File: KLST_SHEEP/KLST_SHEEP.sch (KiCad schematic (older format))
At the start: 55 parts, among them J1 Micro_SD_Card_Card_Detect_SPI, J11 GPIO_EXT_A, J13 GPIO_EXT_B, J14 GPIO_EXT_C, J2 USB_A, J3 USB_B_Micro, J4 GPIO+AUDIO+ANALOG, J5 ARM_JTAG_SWD(STDC14), Q1 AO3401A, SW1 BUTTON_BOOT_FLASH, SW2 BUTTON_RESET, U1 STM32H743VITx, U2 AMS1117-3.3, X1 KLST_SHEEP--graphics, Y1 16MHz

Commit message: minor changes
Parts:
- removed C49: 100nF, Capacitor_SMD:C_0402_1005Metric, symbol Device:C_Small
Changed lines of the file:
@@
 Wire Wire Line
 	3050 14250 2600 14250
-$Comp
-L Device:C_Small C49
-U 1 1 616FFCC3
-P 3500 14100
-F 0 "C49" H 3592 14146 50  0000 L CNN
-F 1 "100nF" H 3592 14055 50  0000 L CNN
-F 2 "Capacitor_SMD:C_0402_1005Metric" H 3500 14100 50  0001 C CNN
-F 3 "~" H 3500 14100 50  0001 C CNN
-F 4 "CL05B104KO5NNNC" H 3500 14100 50  0001 C CNN "MFR.Part #"
-F 5 "C1525" H 3500 14100 50  0001 C CNN "LCSC Part #"
-F 6 "-" H 3500 14100 50  0001 C CNN "Extended Part"
-	1    3500 14100
-	1    0    0    -1
-$EndComp
-Wire Wire Line
-	3050 13950 3500 13950
-Wire Wire Line
-	3500 13950 3500 14000
-Wire Wire Line
-	3500 14200 3500 14250
-Wire Wire Line
-	3500 14250 3050 14250
 Connection ~ 2600 13950
 Connection ~ 2600 14250
-Connection ~ 3050 13950
-Connection ~ 3050 14250
 Text Label 2250 2850 2    50   ~ 0
 RCC_OSC_IN

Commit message: added NHD display
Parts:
- removed J5: ARM_JTAG_SWD(STDC14), Connector_PinHeader_1.27mm:PinHeader_2x07_P1.27mm_Vertical_SMD, symbol Connector:Conn_ST_STDC14
- added C12, C3, C5: 1uF, Capacitor_SMD:C_0402_1005Metric, symbol Device:C_Small
- added C4, C6, C7, C8, C9: 100nF, Capacitor_SMD:C_0402_1005Metric, symbol Device:C_Small
- added DS1: NHD-C12832A1Z-FSW-FBW-3V3, KLST_TINY:Newhaven_Display-NHD-C12832A1Z-FSW-FBW-3V3, symbol Newhaven_Display-NHD-C12832A1Z-FSW-FBW-3V3:NHD-C12832A1Z-FSW-FBW-3V3
- added J8: ARM_JTAG_SWD(STDC14), Connector_PinHeader_1.27mm:PinHeader_2x07_P1.27mm_Vertical_SMD, symbol Connector:Conn_ST_STDC14
- added R12: R_Small, Resistor_SMD:R_0805_2012Metric, symbol Device:R_Small
- renumbered C4 to C10, C5 to C11, C7 to C13, C8 to C14, C45 to C15, C46 to C16, C47 to C17, C9 to C18, C10 to C19, C11 to C20, C12 to C21, C13 to C22, C14 to C23, C15 to C24, C48 to C25, C6 to C26, J4 to J2, J2 to J3, J11 to J4, J3 to J5, J13 to J6, J14 to J7, R8 to R10, R9 to R11, R47 to R2, R2 to R3, R48 to R4, R4 to R5, R5 to R6, R6 to R7, R7 to R8, R3 to R9
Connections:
- net SWD_SWI is gone; now on net GPIO_EXT_A_07: U1.77 (PA15)
- net +3V3: now also DS1.12 (VDD), J8.3 (VCC), R12.2
- net GND: now also C12.2, C4.2, C6.2, C7.2, C8.2, C9.2, DS1.11 (VSS), DS1.K (LED-), J8.11 (GNDDetect), J8.5 (GND), J8.7 (GND)
- net GPIO_EXT_A_00: now also U1.84 (PD3); no longer U1.85 (PD4)
- net GPIO_EXT_A_01: now also U1.83 (PD2); no longer U1.84 (PD3)
- net GPIO_EXT_A_02: now also U1.82 (PD1), DS1.16 (~RST~); no longer U1.83 (PD2)
- net GPIO_EXT_A_03: now also U1.81 (PD0), DS1.15 (A0); no longer U1.82 (PD1)
- net GPIO_EXT_A_04: now also U1.80 (PC12), DS1.13 (SI); no longer U1.81 (PD0)
- net GPIO_EXT_A_05: now also U1.79 (PC11); no longer U1.80 (PC12)
- net GPIO_EXT_A_06: now also U1.78 (PC10), DS1.14 (SCL); no longer U1.79 (PC11)
- net GPIO_EXT_A_07: now also DS1.17 (~CS1~); no longer U1.78 (PC10)
- net SERIAL_DEBUG_RX: now also J8.14 (VCP_TX)
- net SERIAL_DEBUG_TX: now also J8.13 (VCP_RX)
- net SWD_NRST: now also J8.12 (~RST)
- net SWD_SWCLK: now also J8.6 (JCLK/SWCLK)
- net SWD_SWDIO: now also J8.4 (JTMS/SWDIO)
- net SWD_SWO: now also J8.8 (JTDO/SWO)
- new net: C4.1, DS1.1 (V0)
- new net: C12.1, DS1.10 (VOUT)
- new net: C6.1, DS1.2 (V1)
- new net: C7.1, DS1.3 (V2)
- new net: C8.1, DS1.4 (V3)
- new net: C9.1, DS1.5 (V4)
- new net: C5.2, DS1.6 (C2-)
- new net: C5.1, DS1.7 (C2+)
- new net: C3.1, DS1.8 (C1+)
- new net: C3.2, DS1.9 (C1-)
- new net: DS1.A (LED+), R12.1
- no-connect marks 4 -> 6
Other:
- note added: "EXTERNAL_DISPLAY\n"
- note added: "PITCH=1.5mm"
- note added: "https://www.newhavendisplay.com/nhdpcb12832a1z-p-3569.html"

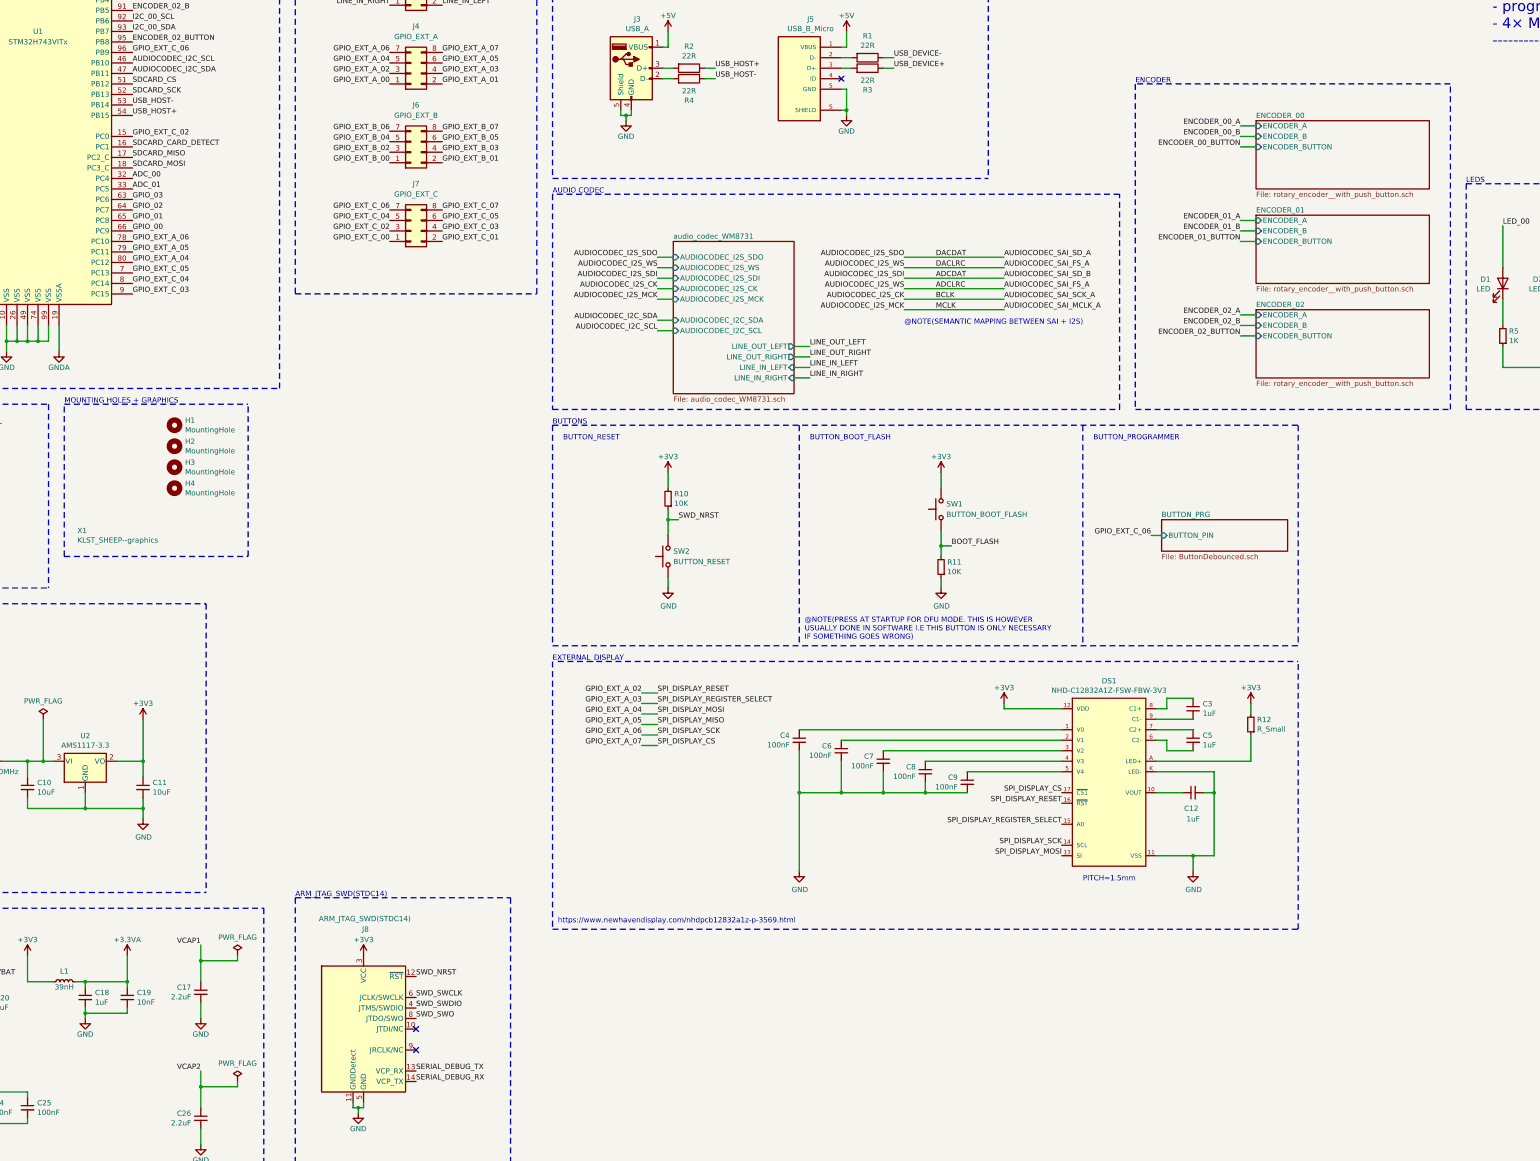
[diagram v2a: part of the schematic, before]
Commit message: added screen, added icon
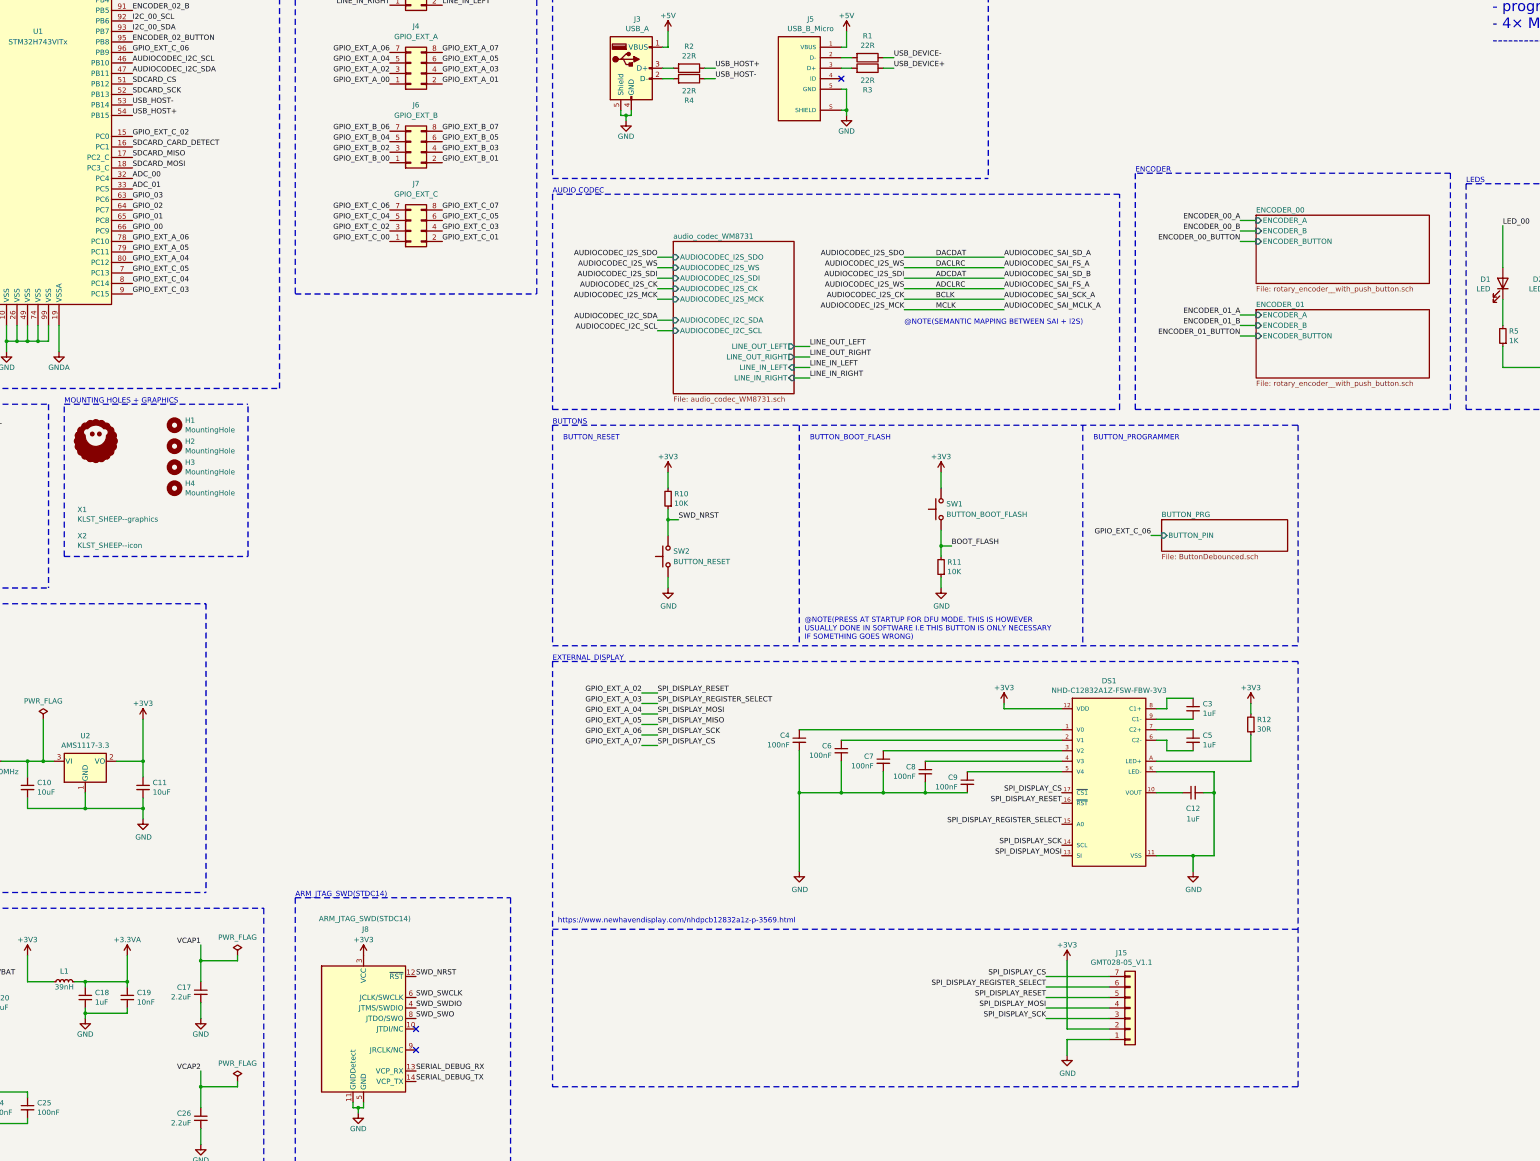
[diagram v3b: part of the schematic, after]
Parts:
- added J15: GMT028-05_V1.1, Connector_PinSocket_2.54mm:PinSocket_1x07_P2.54mm_Vertical, symbol Connector_Generic:Conn_01x07
- added X2: KLST_SHEEP--icon, KLST_TINY:KLST_SHEEP--icon, symbol KLST_SHEEP--graphics:KLST_SHEEP--graphics
- R12: value R_Small -> 30R
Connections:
- net +3V3: now also J15.2 (Pin_2)
- net GND: now also J15.1 (Pin_1)
- net GPIO_EXT_A_02: now also J15.5 (Pin_5)
- net GPIO_EXT_A_03: now also J15.6 (Pin_6)
- net GPIO_EXT_A_04: now also J15.4 (Pin_4)
- net GPIO_EXT_A_06: now also J15.3 (Pin_3)
- net GPIO_EXT_A_07: now also J15.7 (Pin_7)
- net SERIAL_DEBUG_RX: now also J8.13 (VCP_RX); no longer J8.14 (VCP_TX)
- net SERIAL_DEBUG_TX: now also J8.14 (VCP_TX); no longer J8.13 (VCP_RX)
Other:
- note removed: "PITCH=1.5mm"
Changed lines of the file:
@@
 $Descr A2 23386 16535
 encoding utf-8
-Sheet 1 7
+Sheet 1 6
 Title "KLST_SHEEP"
 Date "2021-10-11"
@@
 Text Notes 800  7400 0    50   ~ 0
 XTAL
-Text Label 14600 4850 2    50   ~ 0
+Text Label 14600 5750 2    50   ~ 0
 ENCODER_00_B
-Text Label 14600 4750 2    50   ~ 0
+Text Label 14600 5650 2    50   ~ 0
 ENCODER_00_A
-Text Label 14600 4950 2    50   ~ 0
+Text Label 14600 5850 2    50   ~ 0
 ENCODER_00_BUTTON
-Text Label 14600 5750 2    50   ~ 0
+Text Label 14600 6650 2    50   ~ 0
 ENCODER_01_B
-Text Label 14600 5650 2    50   ~ 0
+Text Label 14600 6550 2    50   ~ 0
 ENCODER_01_A
-Text Label 14600 5850 2    50   ~ 0
+Text Label 14600 6750 2    50   ~ 0
 ENCODER_01_BUTTON
-Text Label 14600 6650 2    50   ~ 0
-ENCODER_02_B
-Text Label 14600 6550 2    50   ~ 0
-ENCODER_02_A
-Text Label 14600 6750 2    50   ~ 0
-ENCODER_02_BUTTON
-Wire Notes Line
-	16600 4350 13600 4350
-Text Notes 13600 4350 0    50   ~ 0
+Wire Notes Line
+	16600 5200 13600 5200
+Text Notes 13600 5200 0    50   ~ 0
 ENCODER
 $Comp
@@
 $EndComp
 $Sheet
-S 14750 4700 1650 650
+S 14750 5600 1650 650
 U 60628872
 F0 "ENCODER_00" 50
-F1 "rotary_encoder__with_push_button.sch" 50
-F2 "ENCODER_BUTTON" I L 14750 4950 50
-F3 "ENCODER_B" I L 14750 4850 50
-F4 "ENCODER_A" I L 14750 4750 50
-$EndSheet
-$Sheet
-S 14750 5600 1650 650
-U 6075A95B
-F0 "ENCODER_01" 50
 F1 "rotary_encoder__with_push_button.sch" 50
 F2 "ENCODER_BUTTON" I L 14750 5850 50
@@
 $Sheet
 S 14750 6500 1650 650
-U 607910C2
-F0 "ENCODER_02" 50
+U 6075A95B
+F0 "ENCODER_01" 50
 F1 "rotary_encoder__with_push_button.sch" 50
 F2 "ENCODER_BUTTON" I L 14750 6750 50
@@
 $EndSheet
 Wire Wire Line
+	14600 5650 14750 5650
+Wire Wire Line
+	14600 5750 14750 5750
+Wire Wire Line
+	14600 5850 14750 5850
+Wire Wire Line
 	14600 6550 14750 6550
 Wire Wire Line
@@
 Wire Wire Line
 	14600 6750 14750 6750
-Wire Wire Line
-	14600 4750 14750 4750
-Wire Wire Line
-	14600 4850 14750 4850
-Wire Wire Line
-	14600 4950 14750 4950
-Wire Wire Line
-	14600 5650 14750 5650
-Wire Wire Line
-	14600 5750 14750 5750
-Wire Wire Line
-	14600 5850 14750 5850
 Text Notes 800  9300 0    50   ~ 0
 VOLTAGE REGULATORS
@@
 	13600 7450 16600 7450
 Wire Notes Line
-	16600 7450 16600 4350
-Wire Notes Line
-	13600 4350 13600 7450
+	16600 7450 16600 5200
+Wire Notes Line
+	13600 5200 13600 7450
 Text Label 4050 1850 0    50   ~ 0
 DAC_00
@@
 L KLST_SHEEP--graphics:KLST_SHEEP--graphics X1
 U 1 1 61CD293A
-P 3500 8650
-F 0 "X1" H 3525 8696 50  0000 L CNN
-F 1 "KLST_SHEEP--graphics" H 3525 8605 50  0000 L CNN
-F 2 "KLST_SHEEP:KLST_SHEEP--graphics" H 3500 8650 100 0001 C CNN
-F 3 "" H 3500 8650 100 0001 C CNN
-F 4 "DNF" H 3500 8650 50  0001 C CNN "MFR.Part #"
-F 5 "-" H 3500 8650 50  0001 C CNN "Extended Part"
-F 6 "DNF" H 3500 8650 50  0001 C CNN "LCSC Part #"
-	1    3500 8650
+P 3500 8450
+F 0 "X1" H 3525 8496 50  0000 L CNN
+F 1 "KLST_SHEEP--graphics" H 3525 8405 50  0000 L CNN
+F 2 "KLST_SHEEP:KLST_SHEEP--graphics" H 3500 8450 100 0001 C CNN
+F 3 "" H 3500 8450 100 0001 C CNN
+F 4 "DNF" H 3500 8450 50  0001 C CNN "MFR.Part #"
+F 5 "-" H 3500 8450 50  0001 C CNN "Extended Part"
+F 6 "DNF" H 3500 8450 50  0001 C CNN "LCSC Part #"
+	1    3500 8450
 	1    0    0    -1
 $EndComp
@@
 Text Label 2250 5350 2    50   ~ 0
 SERIAL_DEBUG_TX
+Text Label 6750 13750 0    50   ~ 0
+SERIAL_DEBUG_RX
 Text Label 6750 13850 0    50   ~ 0
-SERIAL_DEBUG_RX
-Text Label 6750 13750 0    50   ~ 0
 SERIAL_DEBUG_TX
 Text Label 4050 2750 0    50   ~ 0
@@
 SPI_DISPLAY_CS
 Wire Notes Line
-	8050 9850 8050 12400
+	8050 9850 8050 13900
 Text Notes 8050 9850 0    50   ~ 0
 EXTERNAL_DISPLAY\n
 Wire Notes Line
-	8100 9850 15150 9850
+	8050 9850 15150 9850
 Wire Wire Line
 	8900 10150 9050 10150
@@
 	8900 10650 9050 10650
 Wire Notes Line
-	15150 12400 15150 9850
-Text Notes 13100 11950 0    50   ~ 0
-PITCH=1.5mm
+	15150 13900 15150 9850
 Text Notes 8100 12350 0    50   ~ 0
 https://www.newhavendisplay.com/nhdpcb12832a1z-p-3569.html
@@
 P 14700 10450
 F 0 "R12" H 14641 10404 50  0000 R CNN
-F 1 "R_Small" H 14641 10495 50  0000 R CNN
+F 1 "30R" H 14641 10495 50  0000 R CNN
 F 2 "Resistor_SMD:R_0805_2012Metric" H 14700 10450 50  0001 C CNN
 F 3 "~" H 14700 10450 50  0001 C CNN
@@
 U 1 1 619DF4A5
 P 14150 11100
-F 0 "C12" V 14000 11050 50  0000 L CNN
+F 0 "C12" V 14000 11100 50  0000 C CNN
 F 1 "1uF" V 13900 11100 50  0000 C CNN
 F 2 "Capacitor_SMD:C_0402_1005Metric" H 14150 11100 50  0001 C CNN
@@
 	0    -1   -1   0
 $EndComp
+$Comp
+L Connector_Generic:Conn_01x07 J15
+U 1 1 61897A0C
+P 13550 13150
+F 0 "J15" H 13468 12625 50  0000 C CNN
+F 1 "GMT028-05_V1.1" H 13468 12716 50  0000 C CNN
+F 2 "Connector_PinSocket_2.54mm:PinSocket_1x07_P2.54mm_Vertical" H 13550 13150 50  0001 C CNN
+F 3 "~" H 13550 13150 50  0001 C CNN
+	1    13550 13150
+	1    0    0    1
+$EndComp
+Wire Notes Line
+	8050 13900 15150 13900
+$Comp
+L power:GND #PWR081
+U 1 1 61931D21
+P 12950 13600
+F 0 "#PWR081" H 12950 13350 50  0001 C CNN
+F 1 "GND" H 12955 13427 50  0000 C CNN
+F 2 "" H 12950 13600 50  0001 C CNN
+F 3 "" H 12950 13600 50  0001 C CNN
+	1    12950 13600
+	1    0    0    -1
+$EndComp
+$Comp
+L power:+3V3 #PWR080
+U 1 1 61932AAD
+P 12950 12700
+F 0 "#PWR080" H 12950 12550 50  0001 C CNN
+F 1 "+3V3" H 12950 12850 50  0000 C CNN
+F 2 "" H 12950 12700 50  0001 C CNN
+F 3 "" H 12950 12700 50  0001 C CNN
+	1    12950 12700
+	1    0    0    -1
+$EndComp
+Wire Wire Line
+	12950 13600 12950 13450
+Wire Wire Line
+	12950 13450 13350 13450
+Wire Wire Line
+	12950 13350 13350 13350
+Wire Wire Line
+	12950 12700 12950 13350
+Text Label 12750 12950 2    50   ~ 0
+SPI_DISPLAY_REGISTER_SELECT
+Text Label 12750 13150 2    50   ~ 0
+SPI_DISPLAY_MOSI
+Text Label 12750 13250 2    50   ~ 0
+SPI_DISPLAY_SCK
+Text Label 12750 12850 2    50   ~ 0
+SPI_DISPLAY_CS
+Text Label 12750 13050 2    50   ~ 0
+SPI_DISPLAY_RESET
+Wire Wire Line
+	13350 12850 12750 12850
+Wire Wire Line
+	13350 12950 12750 12950
+Wire Wire Line
+	13350 13050 12750 13050
+Wire Wire Line
+	13350 13150 12750 13150
+Wire Wire Line
+	13350 13250 12750 13250
+$Comp
+L KLST_SHEEP--icon:LOGO #G1
+U 1 1 6183E666
+P 3700 7750
+F 0 "#G1" H 3700 7439 60  0001 C CNN
+F 1 "LOGO" H 3700 8061 60  0001 C CNN
+F 2 "" H 3700 7750 100 0001 C CNN
+F 3 "" H 3700 7750 100 0001 C CNN
+	1    3700 7750
+	1    0    0    -1
+$EndComp
+$Comp
+L KLST_SHEEP--graphics:KLST_SHEEP--graphics X2
+U 1 1 61845AB5
+P 3500 8700
+F 0 "X2" H 3525 8746 50  0000 L CNN
+F 1 "KLST_SHEEP--icon" H 3525 8655 50  0000 L CNN
+F 2 "KLST_TINY:KLST_SHEEP--icon" H 3500 8700 100 0001 C CNN
+F 3 "" H 3500 8700 100 0001 C CNN
+	1    3500 8700
+	1    0    0    -1
+$EndComp
 $EndSCHEMATC

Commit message: updated capabilites, updated GPIOs
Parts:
- added D? (x5): LED, LED_SMD:LED_0805_2012Metric_Pad1.15x1.40mm_HandSolder, symbol Device:LED
- added R? (x5): 1K, Resistor_SMD:R_0805_2012Metric_Pad1.20x1.40mm_HandSolder, symbol Device:R_Small
- DS1: footprint KLST_TINY:Newhaven_Display-NHD-C12832A1Z-FSW-FBW-3V3 -> KLST_SHEEP:Newhaven_Display-NHD-C12832A1Z-FSW-FBW-3V3
- X2: footprint KLST_TINY:KLST_SHEEP--icon -> KLST_SHEEP:KLST_SHEEP--icon
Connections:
- net GPIO_EXT_A_02: no longer J4.3 (Pin_3)
- net GPIO_EXT_A_03: no longer J4.4 (Pin_4)
- net GPIO_EXT_A_04: no longer J4.5 (Pin_5)
- net GPIO_EXT_A_05: no longer J4.6 (Pin_6)
- net GPIO_EXT_A_06: no longer J4.7 (Pin_7)
- net GPIO_EXT_A_07: no longer J4.8 (Pin_8)
- net ENCODER_02_A: no longer names the net of U1.90 (PB4)
- net ENCODER_02_B: no longer names the net of U1.91 (PB5)
- net ENCODER_02_BUTTON: no longer names the net of U1.95 (PB8)
- new net: D?.1 (K), R?.2 (x5)
- new net LED_03: D?.2 (A)
- new net LED_04: D?.2 (A)
- new net LED_05: D?.2 (A)
- new net LED_06: D?.2 (A)
- new net LED_07: D?.2 (A)
- no-connect marks 6 -> 9
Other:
- moved on the sheet: D4, R8

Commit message: cleaned up
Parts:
- added D? (x8): LED, LED_SMD:LED_0805_2012Metric_Pad1.15x1.40mm_HandSolder, symbol Device:LED
- added R? (x8): 1K, Resistor_SMD:R_0805_2012Metric_Pad1.20x1.40mm_HandSolder, symbol Device:R_Small
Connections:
- net GND: now also R?.1, R?.1, R?.1, R?.1, R?.1, R?.1, R?.1, R?.1, R?.1, R?.1, R?.1, R?.1, R?.1
- net GPIO_EXT_A_02 renamed SPI_DISPLAY_RESET
- net GPIO_EXT_A_03 renamed SPI_DISPLAY_REGISTER_SELECT
- net GPIO_EXT_A_04 renamed SPI_DISPLAY_MOSI
- net GPIO_EXT_A_05 renamed SPI_DISPLAY_MISO
- net GPIO_EXT_A_06 renamed SPI_DISPLAY_SCK
- net GPIO_EXT_A_07 renamed SPI_DISPLAY_CS
- new net: D?.1 (K), R?.2 (x8)
- new net LED_08: D?.2 (A)
- new net LED_09: D?.2 (A)
- new net LED_10: D?.2 (A)
- new net LED_11: D?.2 (A)
- new net LED_12: D?.2 (A)
- new net LED_13: D?.2 (A)
- new net LED_14: D?.2 (A)
- new net LED_15: D?.2 (A)
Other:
- note added: "--------------------------------\nTODO\n--------------------------------\n- [ ] CHECK PINS\n- [ ] ADD SPIs TO *GPIO PORT*\n--------------------------------"

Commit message: added icons
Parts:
- added X3: KLST_SHEEP--wolf, KLST_SHEEP:KLST_SHEEP--wolf, symbol KLST_SHEEP--graphics:KLST_SHEEP--graphics
- X1: footprint KLST_SHEEP:KLST_SHEEP--graphics -> KLST_SHEEP:KLST--icon; Extended Part - -> (none); LCSC Part # DNF -> (none); MFR.Part # DNF -> (none)
- gave numbers to parts that had none: 26
- renumbered D4 to D9, J15 to J8, J8 to J9, R8 to R13, R9 to R14, R10 to R15, R11 to R24, R12 to R25
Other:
- moved on the sheet: H1, H2, H3, H4
